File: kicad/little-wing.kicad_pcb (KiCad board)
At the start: 2 copper layers, 124.1 x 130 mm, 609 parts, among them IC1 AP7335-WG-7, J1 nice!view, J10 rgb, J11 rows, J12 columns, J13 columns, J2 Battery, J3 trackball, J4 trackball, J5 rotary, J6 nice!view, J7 Battery, J8 rgb, J9 rows, SW1 Power, SW2 Reset, SW3 Reset, SW4 Power, U1 nice!nano v2, U2 PMW3610, U3 nice!nano v2

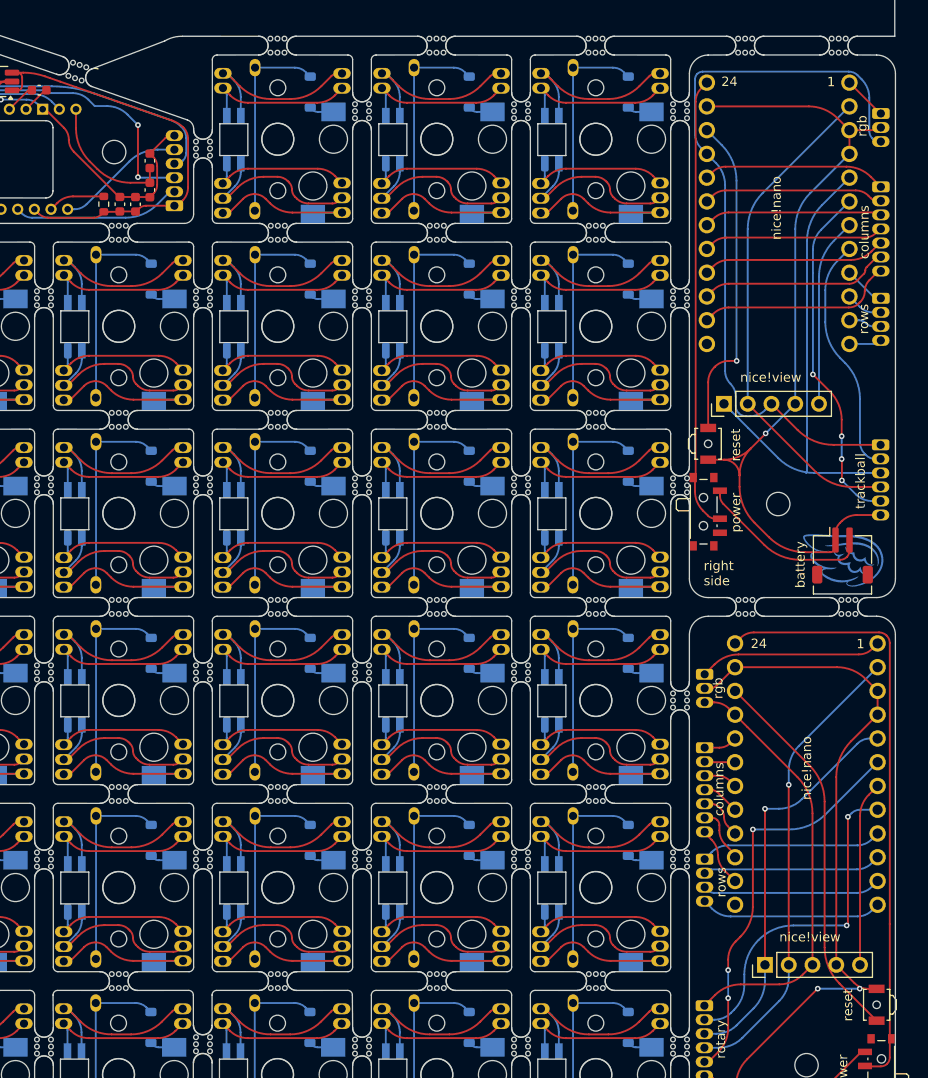
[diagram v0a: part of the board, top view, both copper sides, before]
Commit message: Reworking the schematics for a smaller power stepdown unit
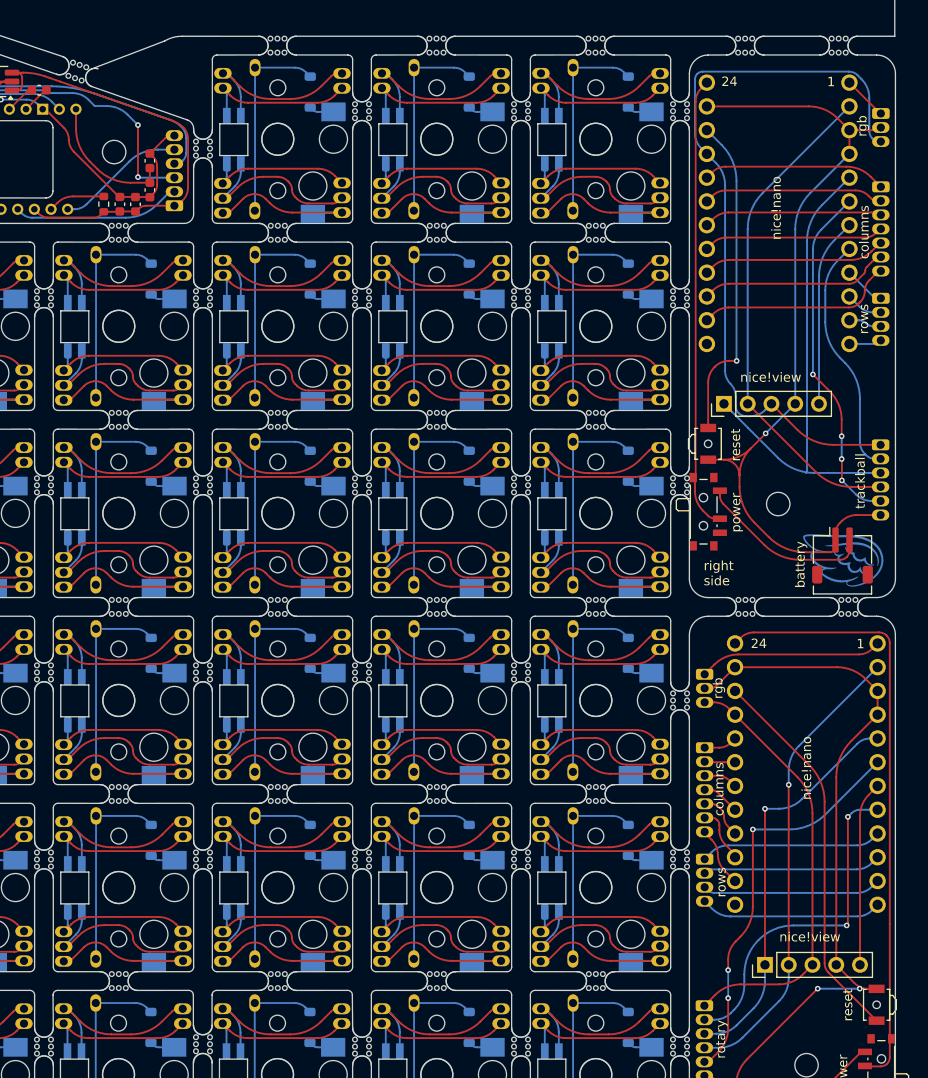
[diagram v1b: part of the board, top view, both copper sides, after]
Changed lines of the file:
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@@
 		(fp_arc
 			(start -2 -1)
-			(mid -1.000001 0)
+			(mid -1.000001 0.000001)
 			(end -2.000002 1)
 			(stroke
@@
 		(fp_arc
 			(start 2 1)
-			(mid 1.000001 0)
+			(mid 0.999999 -0.000001)
 			(end 2.000002 -1)
 			(stroke
@@
 		(fp_arc
 			(start -2.000002 -1)
-			(mid -0.999997 0)
+			(mid -0.999998 -0.000002)
 			(end -1.999999 1.000001)
 			(stroke
@@
 		(fp_arc
 			(start 2.000002 1)
-			(mid 0.999997 0)
+			(mid 0.999998 0.000002)
 			(end 1.999999 -1.000001)
 			(stroke
@@
 	)
 	(segment
-		(start 198.09046 131.275138)
+		(start 196.894928 130.079606)
 		(end 202.058592 135.24327)
 		(width 0.2)
@@
 	)
 	(segment
-		(start 196.496668 127.427382)
+		(start 196.496668 129.118121)
 		(end 196.496668 111.820735)
 		(width 0.2)
@@
 	)
 	(arc
-		(start 196.496668 127.427382)
-		(mid 196.910881 129.509772)
-		(end 198.09046 131.275138)
+		(start 196.496668 129.118121)
+		(mid 196.600172 129.638473)
+		(end 196.894928 130.079606)
 		(width 0.2)
 		(layer "F.Cu")

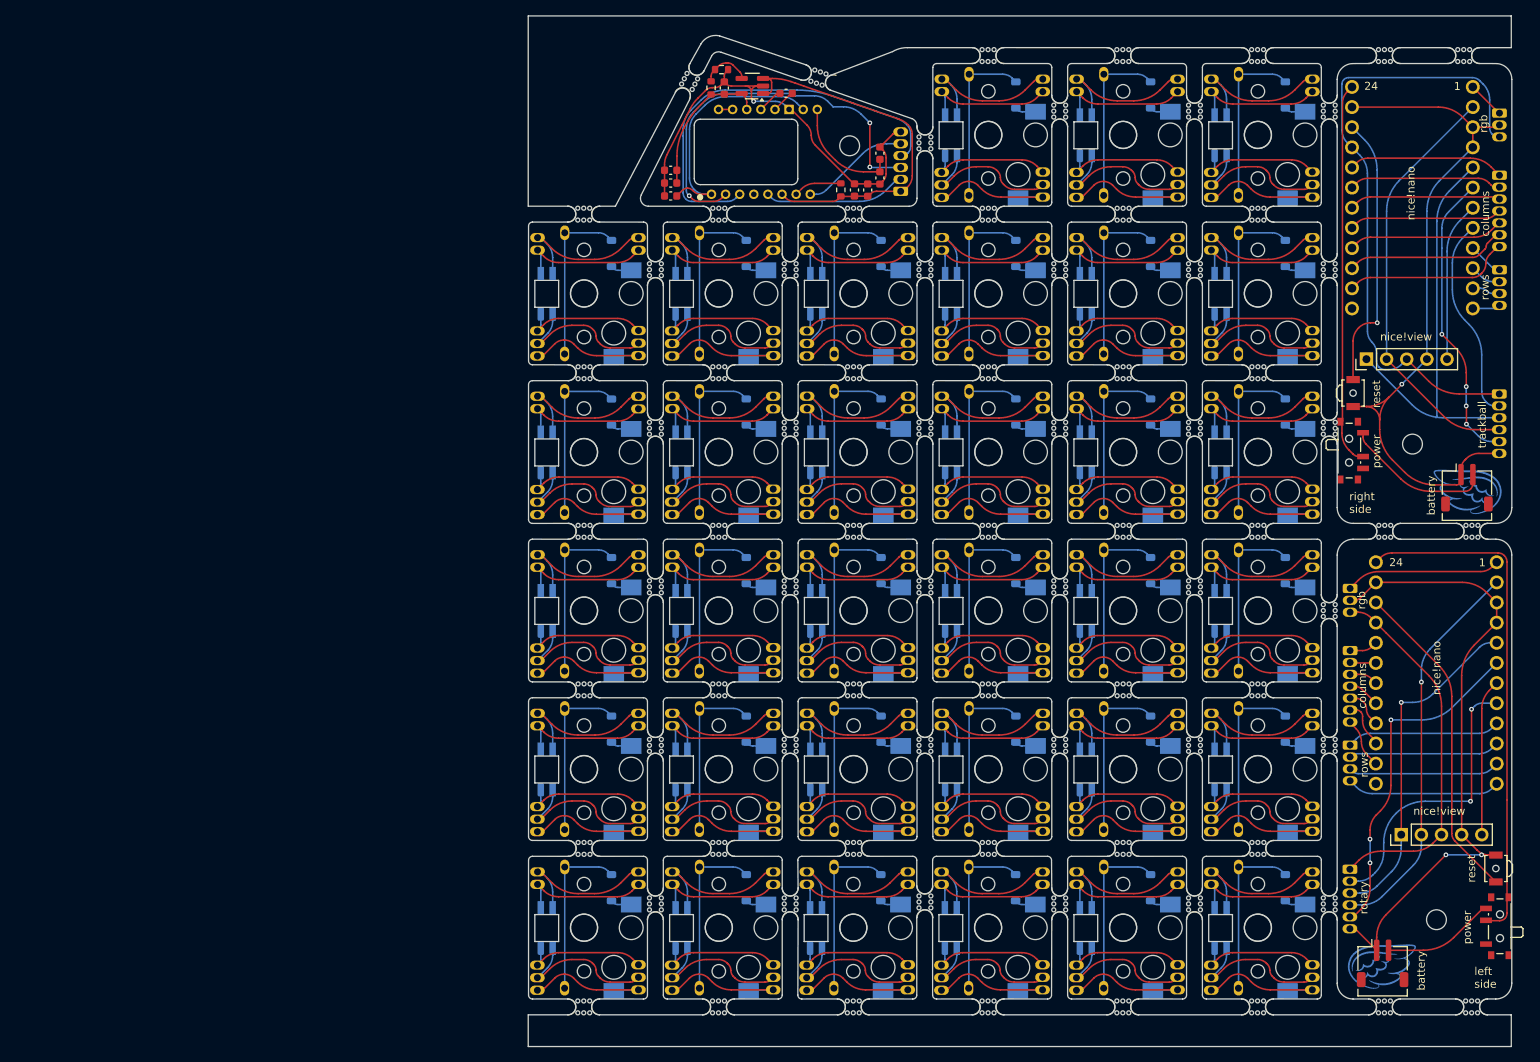
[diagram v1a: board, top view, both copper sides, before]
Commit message: Throwing in the new PCB outline for the optical sensor
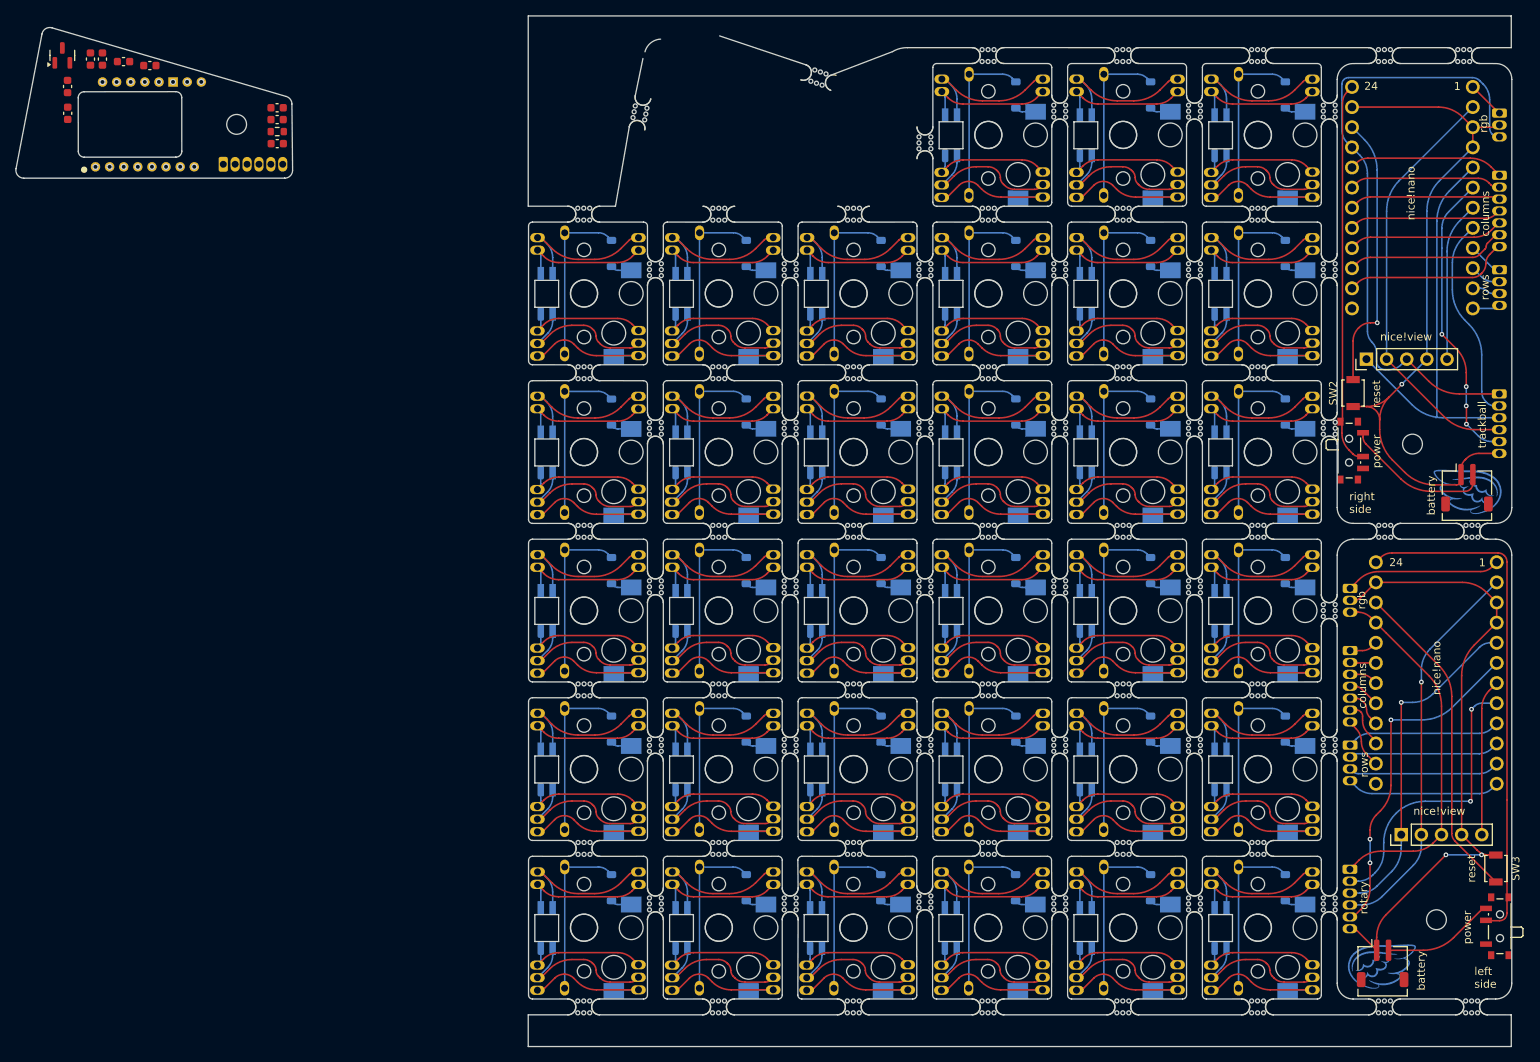
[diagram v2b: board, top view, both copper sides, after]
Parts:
- removed IC1: AP7335-WG-7, Package_TO_SOT_SMD:SOT-23-5_HandSoldering
- removed R2: 10k, Resistor_SMD:R_0603_1608Metric
- removed R3: 15k, Resistor_SMD:R_0603_1608Metric
- added U4: MCP1700x-180xxTT, Package_TO_SOT_SMD:SOT-23, F.Cu at (21.2, 31.0)
- C6: value 100n (X7R) -> 100n (X7R)
- C8: value 10u (X7R) -> 10u (X7R)
- C9: value 10n (X7R) -> 10n (X7R)
- J4: value trackball -> rotary
- J5: value rotary -> trackball
- SW2, SW3: footprint Button_Switch_SMD:SW_SPST_B3U-3000P-B -> Button_Switch_SMD:SW_SPST_B3U-1000P
- moved C11 101.4 mm to (21.9, 38.3)
- moved J3 85.5 mm to (41.5, 44.7), turned to 0 degrees
- moved C6 83.7 mm to (28.9, 31.8), turned to -5.68989e-15 degrees
- moved C10 82.8 mm to (21.9, 34.9), turned to -90 degrees
- moved U2 77.8 mm to (29.7, 39.7)
- moved C8 76.4 mm to (48.3, 39.1), turned to 0 degrees
- moved C9 76.3 mm to (48.3, 37.6), turned to -5.68989e-15 degrees
- moved C2 74.5 mm to (24.8, 31.4), turned to 90 degrees
- moved C3 73.4 mm to (26.3, 31.4), turned to 90 degrees
- moved C7 73.0 mm to (48.3, 42.1), turned to 0 degrees
- moved R1 71.5 mm to (48.3, 40.6), turned to 180 degrees
- moved C1 67.7 mm to (32.3, 32.3)
- moved mouse-bite-2mm-slot 7.41 mm to (94.1, 38.2), turned to 79.1 degrees
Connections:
- net +1V9 renamed +1V8
- net MISO L renamed IRQ L
- net MISO R renamed IRQ R
- net MOSI L renamed SDIO L
- net MOSI R renamed SDIO R
- net MOTION renamed IRQ
- SW1 pad : BAT L -> (no net)
- SW4 pad : BAT R -> (no net)
- SW4 pad 1: (no net) -> Net-(J7-Pin_2)
- SW4 pad 3: Net-(J7-Pin_2) -> (no net)
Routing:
- net GND: track 585.4 -> 527.7 mm, vias 1 -> 0
- net SCLK: track 52.3 -> 0.00 mm
- net SDIO: track 49.8 -> 0.00 mm, vias 3 -> 0
- net 3.3v: track 47.0 -> 0.00 mm
- net Net-(U2-+VCSEL): track 31.9 -> 0.00 mm
- net +1V8: track 18.6 -> 0.00 mm
- net NCS: track 17.9 -> 0.00 mm
- net Net-(U2-VCP): track 14.7 -> 0.00 mm
- net IRQ: track 13.8 -> 0.00 mm
- net Net-(IC1-ADJ): track 6.37 -> 0.00 mm
- net Net-(U2-NRESET): track 6.10 -> 0.00 mm
- net Net-(U2-CN): track 3.23 -> 0.00 mm
- net Net-(U2-CP): track 3.02 -> 0.00 mm
- net Net-(U2--VCSEL): track 1.78 -> 0.00 mm
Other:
- board size 124.1 x 130 mm -> 188.7 x 130 mm

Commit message: Stashing work
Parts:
- moved C8 1.62 mm to (47.2, 37.9), turned to -90 degrees
- moved C6 0.57 mm to (29.2, 32.3)
- moved C9 0.48 mm to (48.7, 37.9), turned to -90 degrees
- moved R1 0.40 mm to (47.9, 40.6)
- moved C7 0.40 mm to (47.9, 42.1)
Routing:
- net 3.3v: track 0.00 -> 46.9 mm
- net GND: track 527.7 -> 573.9 mm
- net Net-(U2-+VCSEL): track 0.00 -> 31.6 mm
- net Net-(U2-NRESET): track 0.00 -> 15.2 mm
- net NCS: track 0.00 -> 11.6 mm
- net IRQ: track 0.00 -> 11.3 mm
- net +1V8: track 0.00 -> 11.0 mm
- net Net-(U2-VCP): track 0.00 -> 10.7 mm
- net Net-(U2-CP): track 0.00 -> 4.28 mm
- net Net-(U2-CN): track 0.00 -> 4.05 mm
- net Net-(U2--VCSEL): track 0.00 -> 1.78 mm
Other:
- outline, holes or cut-outs redrawn
